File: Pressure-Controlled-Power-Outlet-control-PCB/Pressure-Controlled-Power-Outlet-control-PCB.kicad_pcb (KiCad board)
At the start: 4 copper layers, 100.3 x 100.3 mm, 49 parts, among them J1 pressure sensor, J2 1017514, J3 I2C0 Connector, J4 SPI1 Connector, J5 FanA 5V/12V, J6 FanB 5V/12V, K1 T9GV5L24-24, K2 T9GV5L24-24, M1 Fan_4pin, M2 Fan_4pin, Q1 2N3906, Q2 IRF540N, Q3 IRF540N, Q4 2N3906, Q5 2N3904, Q6 2N3904, Q7 2N3904, Q8 2N3904, U1 Pico, U2 LM324, U3 LF50_TO220, U4 LM1085-12

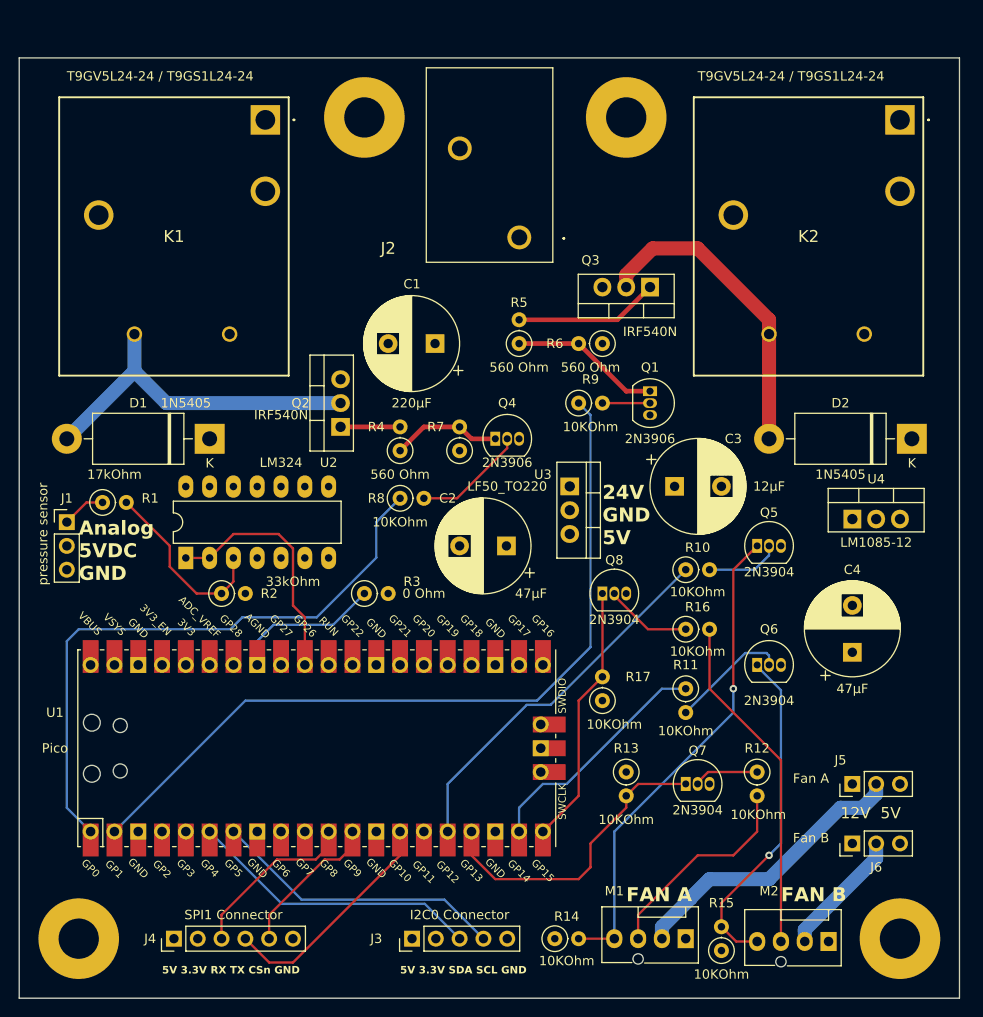
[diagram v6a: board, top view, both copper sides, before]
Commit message: added 5v fan headers
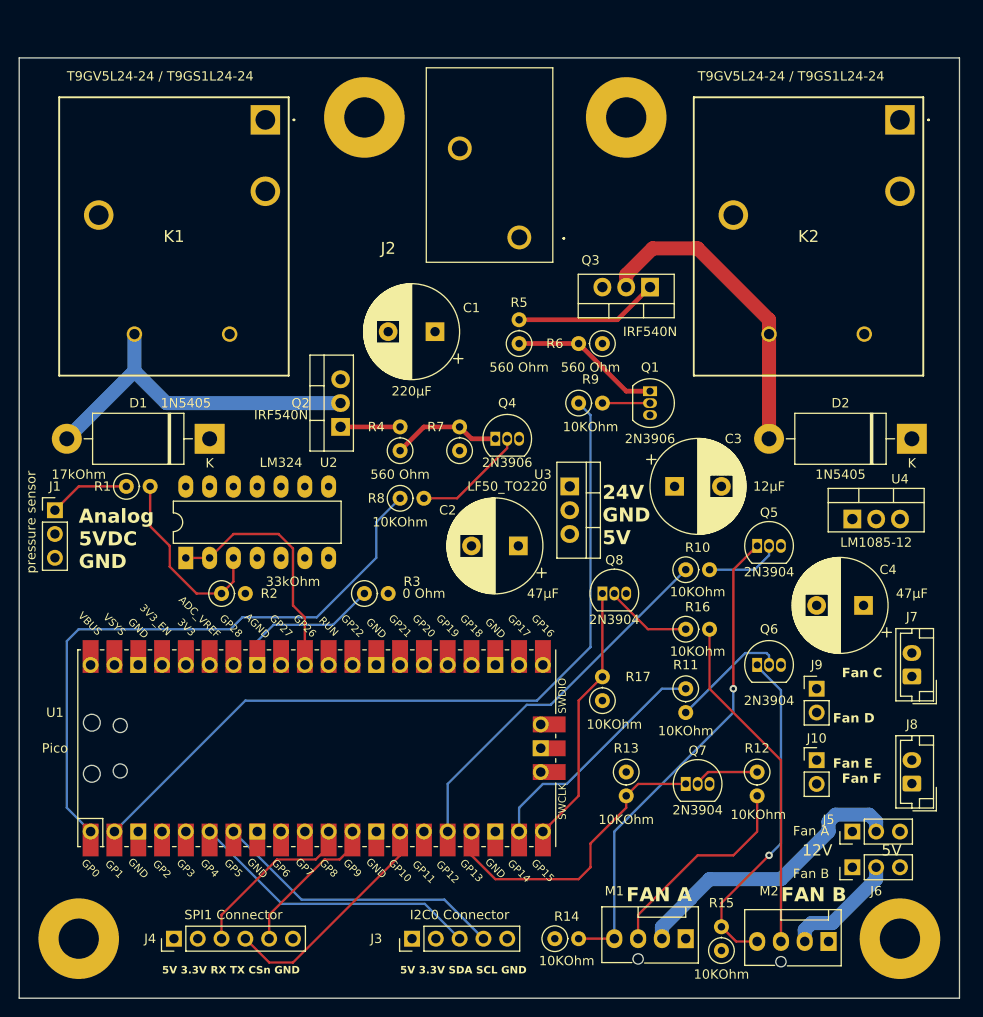
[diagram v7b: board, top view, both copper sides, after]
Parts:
- added J10: Conn_01x02_Pin, Connector_PinHeader_2.54mm:PinHeader_1x02_P2.54mm_Vertical, F.Cu at (171.4, 130.8)
- added J7: Conn_01x02_Pin, Connector_JST:JST_EH_B2B-EH-A_1x02_P2.50mm_Vertical, F.Cu at (181.6, 121.9)
- added J8: Conn_01x02_Pin, Connector_JST:JST_EH_B2B-EH-A_1x02_P2.50mm_Vertical, F.Cu at (181.6, 133.3)
- added J9: Conn_01x02_Pin, Connector_PinHeader_2.54mm:PinHeader_1x02_P2.54mm_Vertical, F.Cu at (171.4, 123.2)
- moved C4 5.14 mm to (176.4, 114.3), turned to 180 degrees
- moved J5 5.08 mm to (175.3, 138.4)
- moved R1 3.06 mm to (97.8, 101.6)
- moved J6 2.54 mm to (175.3, 142.2)
- moved J1 1.80 mm to (90.2, 104.1)
- moved C2 1.27 mm to (139.6, 108.0)
- moved C1 1.27 mm to (130.7, 85.1)
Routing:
- net /Water Pressure 5V: track 4.68 -> 8.67 mm
- net +12V: track 35.7 -> 38.2 mm
- net /FanB_Power: track 13.6 -> 12.4 mm
- net Net-(U2A-+): track 19.8 -> 20.5 mm
- net +5V: track 25.9 -> 26.5 mm
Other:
- board text added: "Fan C Fan D Fan E Fan F"
